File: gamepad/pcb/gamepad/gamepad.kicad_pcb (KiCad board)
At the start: 2 copper layers, 67.8 x 67.8 mm, 13 parts, among them U3 RP2040-ZERO

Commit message: upt: pcb
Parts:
- moved joystick_right1 46.0 mm to (127.5, 33.5)
- moved joystick_left1 45.8 mm to (81.0, 41.5)
- moved cardinal_down1 13.0 mm to (81.0, 68.0)
- moved cardinal_left1 13.0 mm to (81.0, 59.0)
- moved cardinal_right1 13.0 mm to (81.0, 77.0)
- moved cardinal_up1 13.0 mm to (81.0, 86.0)
- moved dPad_east1 13.0 mm to (127.5, 74.5)
- moved dPad_north1 13.0 mm to (127.5, 83.8)
- moved dPad_south1 13.0 mm to (127.5, 65.5)
- moved dPad_west1 13.0 mm to (127.5, 56.5)
- moved operators_minus1 13.0 mm to (81.0, 50.0)
- moved operators_plus1 13.0 mm to (127.5, 47.5)
- moved U3 1.32 mm to (104.4, 75.7)
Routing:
- net +3V3: track 50.3 -> 119.5 mm
- net Net-(U3-GP11): track 101.6 -> 35.6 mm
- net GND: track 242.4 -> 282.5 mm
- net Net-(U3-GP28): track 89.5 -> 53.8 mm
- net Net-(U3-GP29): track 20.8 -> 48.1 mm
- net Net-(U3-GP8): track 47.1 -> 63.3 mm
- net Net-(U3-GP9): track 37.2 -> 24.7 mm
- net Net-(U3-GP7): track 29.7 -> 19.5 mm
- net Net-(U3-GP27): track 42.3 -> 52.3 mm
- net Net-(U3-GP26): track 38.1 -> 47.8 mm
- net Net-(U3-GP6): track 23.6 -> 16.8 mm
- net Net-(U3-GP10): track 32.1 -> 38.7 mm
- net Net-(U3-GP3): track 48.1 -> 42.7 mm
- net Net-(U3-GP2): track 42.2 -> 37.1 mm
- net Net-(U3-GP1): track 38.8 -> 34.4 mm
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
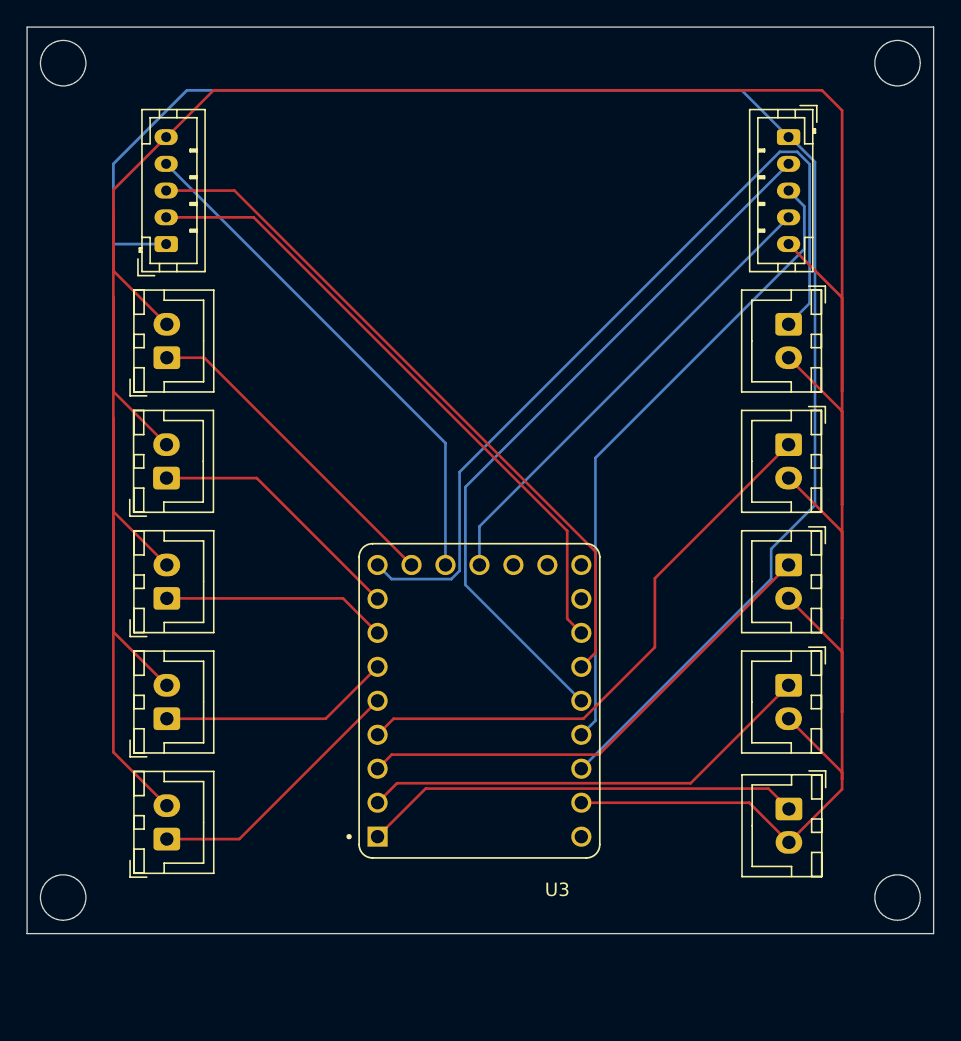
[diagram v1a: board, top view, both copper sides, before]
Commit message: feat: smaller pcb
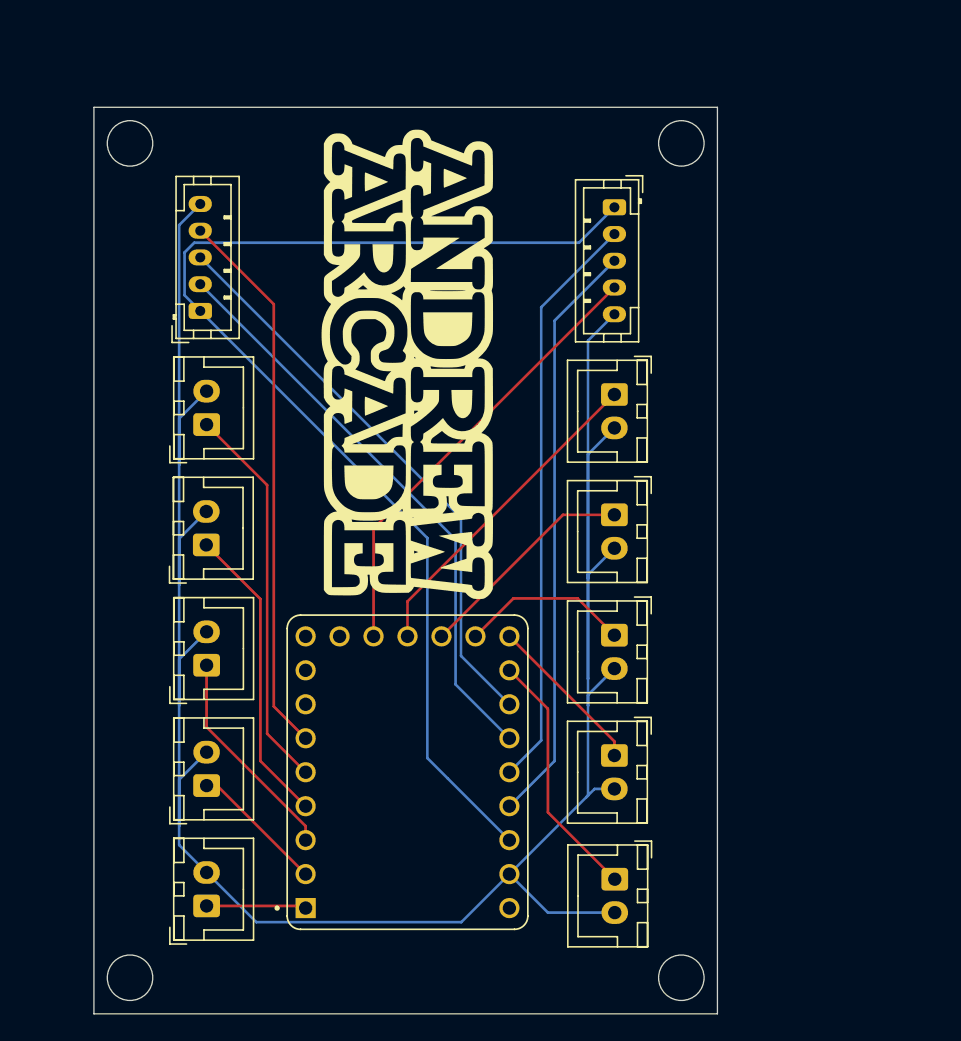
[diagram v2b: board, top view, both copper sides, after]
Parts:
- added G***: LOGO, LOGO, F.Cu at (99.0, 50.5)
- moved dPad_east1 14.0 mm to (114.5, 79.8)
- moved dPad_north1 14.0 mm to (114.5, 89.0)
- moved dPad_south1 14.0 mm to (114.5, 70.8)
- moved dPad_west1 14.0 mm to (114.5, 61.8)
- moved joystick_right1 14.0 mm to (114.5, 38.8)
- moved operators_plus1 14.0 mm to (114.5, 52.8)
- moved U3 7.58 mm to (99.0, 81.0)
- moved cardinal_left1 5.82 mm to (84.0, 64.0)
- moved cardinal_down1 5.82 mm to (84.0, 73.0)
- moved cardinal_right1 5.82 mm to (84.0, 82.0)
- moved cardinal_up1 5.82 mm to (84.0, 91.0)
- moved operators_minus1 5.82 mm to (84.0, 55.0)
- moved joystick_left1 5.61 mm to (83.5, 46.5)
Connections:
- U3 pad 10: Net-(U3-GP9) -> unconnected-(U3-GP9-Pad10)
- U3 pad 13: unconnected-(U3-GP12-Pad13) -> Net-(U3-GP12)
- U3 pad 14: unconnected-(U3-GP13-Pad14) -> Net-(U3-GP13)
- U3 pad 15: unconnected-(U3-GP14-Pad15) -> Net-(U3-GP14)
- U3 pad 16: unconnected-(U3-GP15-Pad16) -> Net-(U3-GP15)
- U3 pad 7: Net-(U3-GP6) -> unconnected-(U3-GP6-Pad7)
- U3 pad 8: Net-(U3-GP7) -> unconnected-(U3-GP7-Pad8)
- U3 pad 9: Net-(U3-GP8) -> unconnected-(U3-GP8-Pad9)
- cardinal_down1 pad 1: Net-(U3-GP6) -> Net-(U3-GP2)
- cardinal_left1 pad 1: Net-(U3-GP7) -> Net-(U3-GP3)
- cardinal_right1 pad 1: Net-(U3-GP5) -> Net-(U3-GP1)
- cardinal_up1 pad 1: Net-(U3-GP4) -> Net-(U3-GP0)
- dPad_east1 pad 1: Net-(U3-GP1) -> Net-(U3-GP14)
- dPad_north1 pad 1: Net-(U3-GP0) -> Net-(U3-GP15)
- dPad_south1 pad 1: Net-(U3-GP2) -> Net-(U3-GP13)
- dPad_west1 pad 1: Net-(U3-GP3) -> Net-(U3-GP12)
- joystick_left1 pad 2: Net-(U3-GP26) -> Net-(U3-GP27)
- joystick_left1 pad 3: Net-(U3-GP27) -> Net-(U3-GP26)
- joystick_left1 pad 4: Net-(U3-GP10) -> Net-(U3-GP5)
- joystick_right1 pad 4: Net-(U3-GP11) -> Net-(U3-GP10)
- operators_minus1 pad 1: Net-(U3-GP9) -> Net-(U3-GP4)
- operators_plus1 pad 1: Net-(U3-GP8) -> Net-(U3-GP11)
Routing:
- net GND: track 282.5 -> 185.3 mm
- net Net-(U3-GP8): track 63.3 -> 0.00 mm
- net +3V3: track 119.5 -> 87.6 mm
- net Net-(U3-GP0): track 32.9 -> 7.47 mm
- net Net-(U3-GP9): track 24.7 -> 0.00 mm
- net Net-(U3-GP1): track 34.4 -> 10.1 mm
- net Net-(U3-GP5): track 17.4 -> 41.2 mm
- net Net-(U3-GP2): track 37.1 -> 16.1 mm
- net Net-(U3-GP3): track 42.7 -> 22.6 mm
- net Net-(U3-GP7): track 19.5 -> 0.00 mm
- net Net-(U3-GP15): track 0.00 -> 18.9 mm
- net Net-(U3-GP6): track 16.8 -> 0.00 mm
- net Net-(U3-GP12): track 0.00 -> 16.7 mm
- net Net-(U3-GP13): track 0.00 -> 12.7 mm
- net Net-(U3-GP14): track 0.00 -> 12.2 mm
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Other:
- board size 67.8 x 67.8 mm -> 46.6 x 67.8 mm

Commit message: fix: swap pcb left/right
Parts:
- renumbered dPad_south1 to cardinal_down1, dPad_west1 to cardinal_left1, dPad_east1 to cardinal_right1, dPad_north1 to cardinal_up1, cardinal_down1 to dPad_down1, cardinal_left1 to dPad_left1, cardinal_right1 to dPad_right1, cardinal_up1 to dPad_up1, joystick_right1 to joystick_left1, joystick_left1 to joystick_right1, operators_plus1 to operators_minus1, operators_minus1 to operators_plus1
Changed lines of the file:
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@@
 		(descr "JST XH series connector, B2B-XH-A (http://www.jst-mfg.com/product/pdf/eng/eXH.pdf), generated with kicad-footprint-generator")
 		(tags "connector JST XH vertical")
-		(property "Reference" "operators_plus1"
+		(property "Reference" "operators_minus1"
 			(at 1.25 -3.55 90)
 			(layer "F.SilkS")
@@
 		(descr "JST XH series connector, B2B-XH-A (http://www.jst-mfg.com/product/pdf/eng/eXH.pdf), generated with kicad-footprint-generator")
 		(tags "connector JST XH vertical")
-		(property "Reference" "dPad_south1"
+		(property "Reference" "cardinal_down1"
 			(at 1.25 -3.55 90)
 			(layer "F.SilkS")
@@
 		(descr "JST XH series connector, B2B-XH-A (http://www.jst-mfg.com/product/pdf/eng/eXH.pdf), generated with kicad-footprint-generator")
 		(tags "connector JST XH vertical")
-		(property "Reference" "cardinal_left1"
+		(property "Reference" "dPad_left1"
 			(at 1.25 -3.55 90)
 			(layer "F.SilkS")
@@
 		(descr "JST PH series connector, B5B-PH-K (http://www.jst-mfg.com/product/pdf/eng/ePH.pdf), generated with kicad-footprint-generator")
 		(tags "connector JST PH vertical")
-		(property "Reference" "joystick_right1"
+		(property "Reference" "joystick_left1"
 			(at 4 -2.9 90)
 			(layer "F.SilkS")
@@
 		(descr "JST XH series connector, B2B-XH-A (http://www.jst-mfg.com/product/pdf/eng/eXH.pdf), generated with kicad-footprint-generator")
 		(tags "connector JST XH vertical")
-		(property "Reference" "operators_minus1"
+		(property "Reference" "operators_plus1"
 			(at 1.25 -3.55 90)
 			(layer "F.SilkS")
@@
 		(descr "JST XH series connector, B2B-XH-A (http://www.jst-mfg.com/product/pdf/eng/eXH.pdf), generated with kicad-footprint-generator")
 		(tags "connector JST XH vertical")
-		(property "Reference" "dPad_west1"
+		(property "Reference" "cardinal_left1"
 			(at 1.25 -3.55 90)
 			(layer "F.SilkS")
@@
 		(descr "JST PH series connector, B5B-PH-K (http://www.jst-mfg.com/product/pdf/eng/ePH.pdf), generated with kicad-footprint-generator")
 		(tags "connector JST PH vertical")
-		(property "Reference" "joystick_left1"
+		(property "Reference" "joystick_right1"
 			(at 4 -2.9 90)
 			(layer "F.SilkS")
@@
 		(descr "JST XH series connector, B2B-XH-A (http://www.jst-mfg.com/product/pdf/eng/eXH.pdf), generated with kicad-footprint-generator")
 		(tags "connector JST XH vertical")
-		(property "Reference" "cardinal_right1"
+		(property "Reference" "dPad_right1"
 			(at 1.25 -3.55 90)
 			(layer "F.SilkS")
@@
 		(descr "JST XH series connector, B2B-XH-A (http://www.jst-mfg.com/product/pdf/eng/eXH.pdf), generated with kicad-footprint-generator")
 		(tags "connector JST XH vertical")
-		(property "Reference" "dPad_east1"
+		(property "Reference" "cardinal_right1"
 			(at 1.25 -3.55 90)
 			(layer "F.SilkS")
@@
 		(descr "JST XH series connector, B2B-XH-A (http://www.jst-mfg.com/product/pdf/eng/eXH.pdf), generated with kicad-footprint-generator")
 		(tags "connector JST XH vertical")
-		(property "Reference" "cardinal_down1"
+		(property "Reference" "dPad_down1"
 			(at 1.25 -3.55 90)
 			(layer "F.SilkS")
@@
 		(descr "JST XH series connector, B2B-XH-A (http://www.jst-mfg.com/product/pdf/eng/eXH.pdf), generated with kicad-footprint-generator")
 		(tags "connector JST XH vertical")
-		(property "Reference" "dPad_north1"
+		(property "Reference" "cardinal_up1"
 			(at 44.75 34.45 90)
 			(layer "F.SilkS")
@@
 		(descr "JST XH series connector, B2B-XH-A (http://www.jst-mfg.com/product/pdf/eng/eXH.pdf), generated with kicad-footprint-generator")
 		(tags "connector JST XH vertical")
-		(property "Reference" "cardinal_up1"
+		(property "Reference" "dPad_up1"
 			(at 1.25 -3.55 90)
 			(layer "F.SilkS")
